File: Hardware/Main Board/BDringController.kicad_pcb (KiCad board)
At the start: 2 copper layers, 144.8 x 131.4 mm, 98 parts, among them J1 AUX GPIO, J10 Module 2, J11 VMot, J12 Module 3, J13 Shift Regs and Motor Drvs, J14 Module 4, J15 Module 5, J16 Micro_SD_Card, J17 Pin, J18 Pin, J19 Pin, J20 Pin, J21 Pin, J22 Pin, J23 RST, J24 RST, J3 Torch module, J4 Jumper, J5 Motor, J6 Module 1, J7 Ext Mot Drv, J8 01x02, J9 THC_Display, U1 ESP32_38p, U10 Y, U11 z, U12 A, U13 B, U14 C, U2 74LVC157A, U3 ESP32_38p, U4 BL8071CLATR33, U5 74AHCT595, U6 74AHCT595, U7 74AHCT595, U8 74AHCT595, U9 X

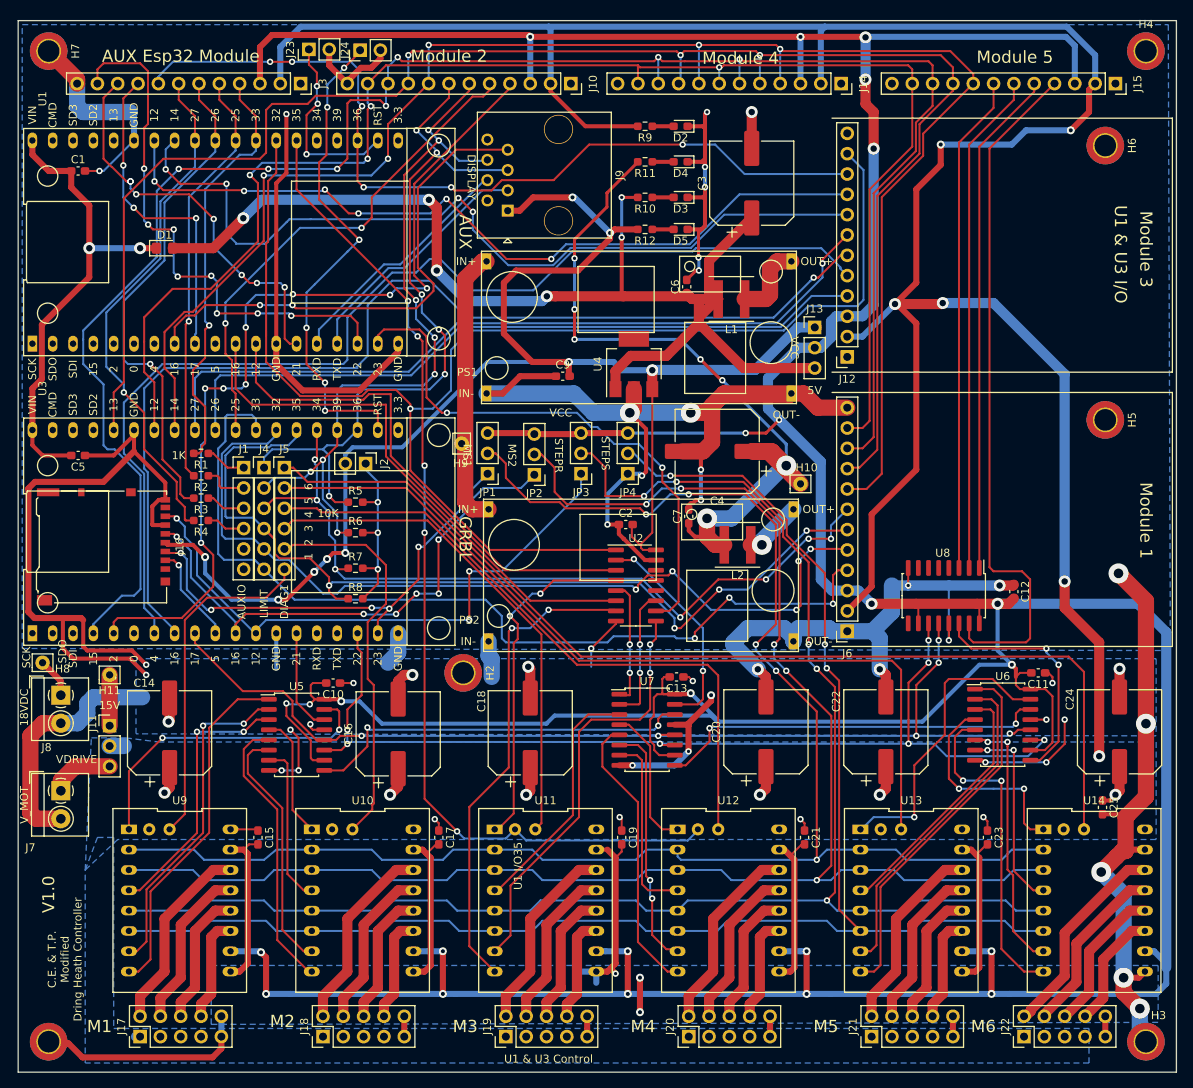
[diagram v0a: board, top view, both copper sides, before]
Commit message: board holder plus ibom
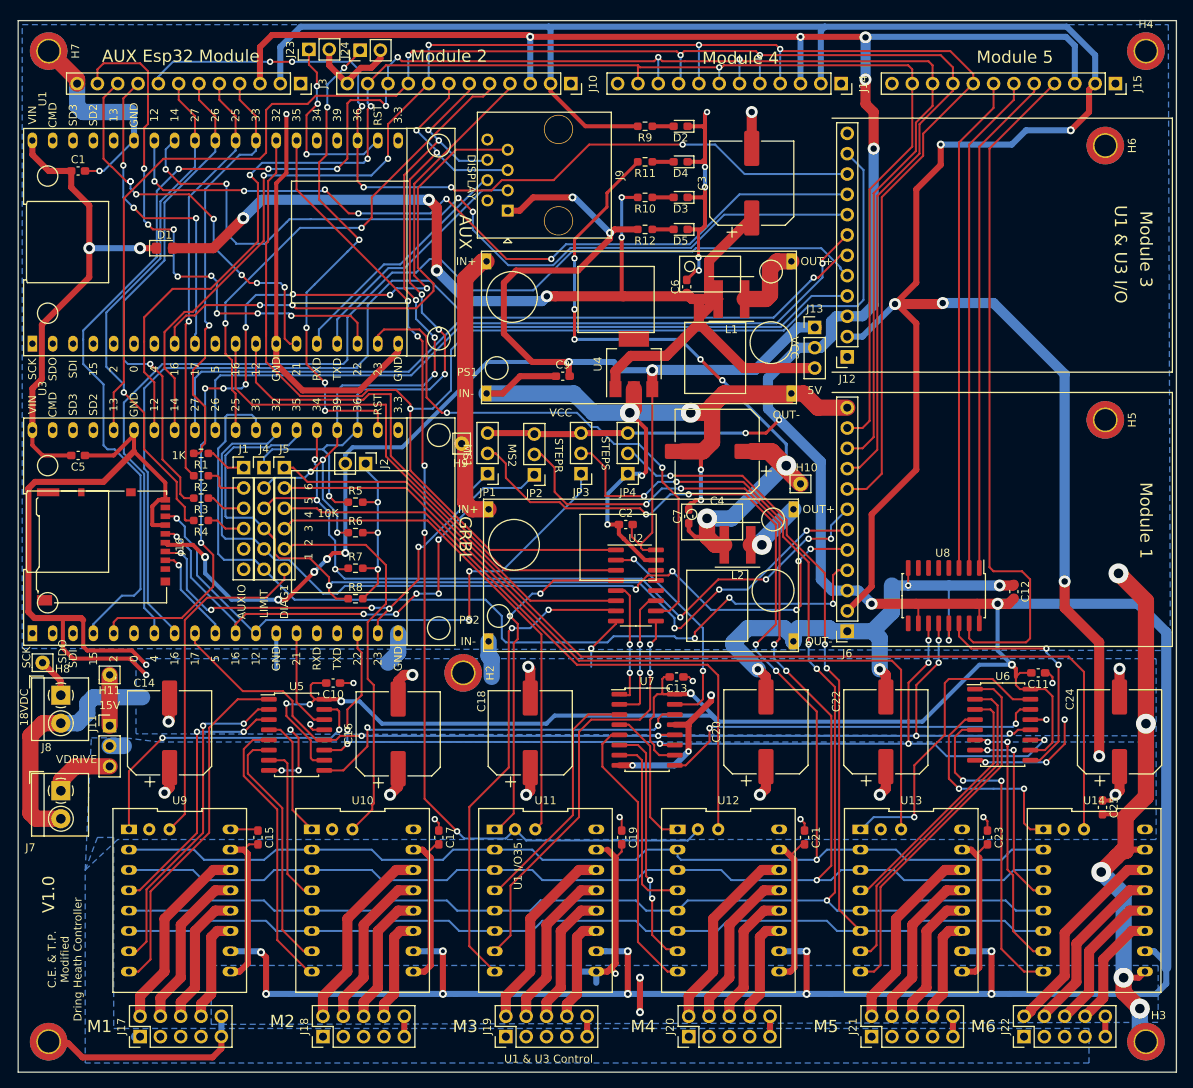
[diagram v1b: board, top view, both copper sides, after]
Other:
- net class 15v removed
- net class Default removed
- board text removed: "V_MOT"
